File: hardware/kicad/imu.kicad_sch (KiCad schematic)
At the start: 5 parts, among them U301 ICM-42688-P

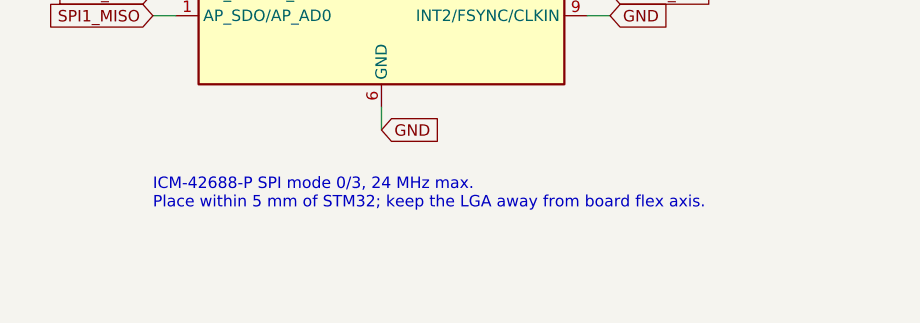
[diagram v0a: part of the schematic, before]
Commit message: Block 3: footprint verification note; ERC severities unchanged
Co-Authored-By: Claude Sonnet 5 <noreply@anthropic.com>
Claude-Session: https://claude.ai/code/session_01JDQYoFvbjRHNSgGtfc2pWo
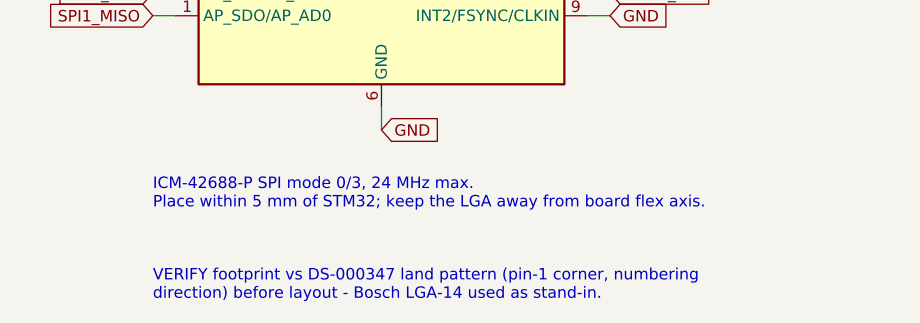
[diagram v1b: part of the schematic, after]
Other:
- note added: "VERIFY footprint vs DS-000347 land pattern (pin-1 corner, numbering direction) before layout - Bosch LGA-14 used as stand-in."
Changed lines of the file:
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@@
+    (effects (font (size 1.27 1.27)) (justify left bottom))
+  )
+  (text "VERIFY footprint vs DS-000347 land pattern (pin-1 corner, numbering\ndirection) before layout - Bosch LGA-14 used as stand-in."
+    (at 139.7 154.94 0)
     (effects (font (size 1.27 1.27)) (justify left bottom))
   )

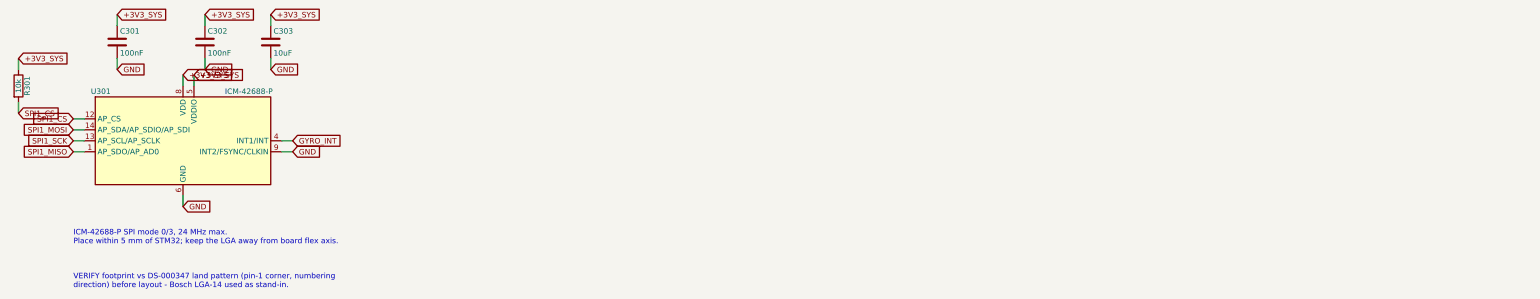
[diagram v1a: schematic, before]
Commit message: Verify IMU footprint; fix Block 7 LED and buzzer parts
- U301 ICM-42688-P footprint verified against DS-000347 Rev 1.2 (LGA-14
  2.5x3.0, 0.5 mm pitch, C-C 2.525/2.025) — Bosch LGA-14 is a correct mate
- D702 S2M 2A silicon in series on J705 strip VDD: drops strip to ~4.3 V so
  WS2812 VIH is reachable from the 3V3 data line
- Q701 2N7002 -> AO3400A for buzzer current headroom
- J705 note records the real limit: ~1 A / ~16 LEDs, capped by the JST-SH

Co-Authored-By: Claude Sonnet 5 <noreply@anthropic.com>
Claude-Session: https://claude.ai/code/session_0171uwNh8K8uwZuWio9f35u1
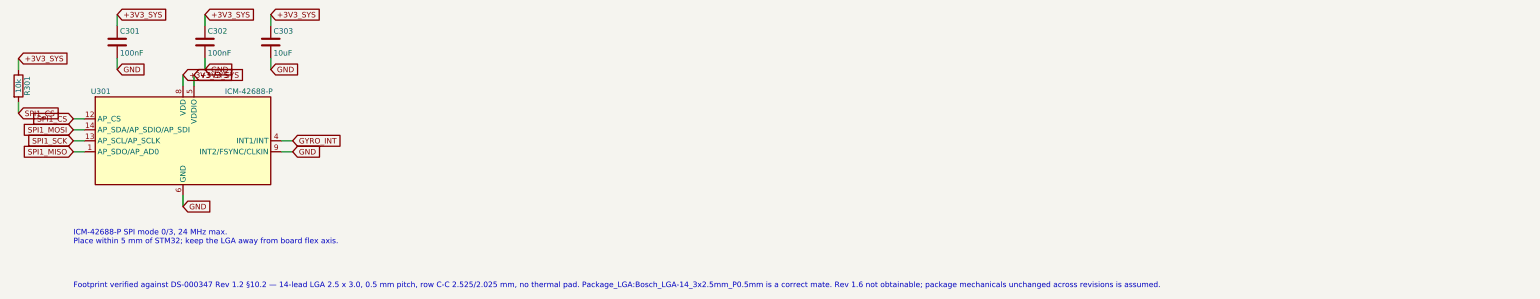
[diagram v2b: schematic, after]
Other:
- note added: "Footprint verified against DS-000347 Rev 1.2 §10.2 — 14-lead LGA 2.5 x 3.0, 0.5 mm pitch, row C-C 2.525/2.025 mm, no thermal pad. Package_LGA:Bosch_LGA-14_3x2.5mm_P0.5mm is a correct mate. Rev 1.6 not obtainable; package mechanicals unchanged across revisions is assumed."
- note removed: "VERIFY footprint vs DS-000347 land pattern (pin-1 corner, numbering direction) before layout - Bosch LGA-14 used as stand-in."
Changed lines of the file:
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@@
     (effects (font (size 1.27 1.27)) (justify left bottom))
   )
-  (text "VERIFY footprint vs DS-000347 land pattern (pin-1 corner, numbering\ndirection) before layout - Bosch LGA-14 used as stand-in."
+  (text "Footprint verified against DS-000347 Rev 1.2 §10.2 — 14-lead LGA 2.5 x 3.0, 0.5 mm pitch, row C-C 2.525/2.025 mm, no thermal pad. Package_LGA:Bosch_LGA-14_3x2.5mm_P0.5mm is a correct mate. Rev 1.6 not obtainable; package mechanicals unchanged across revisions is assumed."
     (at 139.7 154.94 0)
     (effects (font (size 1.27 1.27)) (justify left bottom))
